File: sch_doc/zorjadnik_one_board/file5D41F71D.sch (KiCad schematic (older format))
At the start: 13 parts, among them U3 74HC595, U4 74HC595

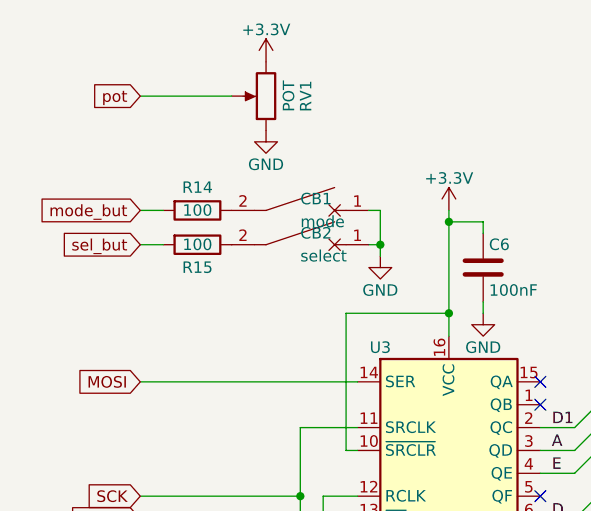
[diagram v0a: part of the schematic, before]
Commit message: полирнул меню, теперь есть функция выкючения
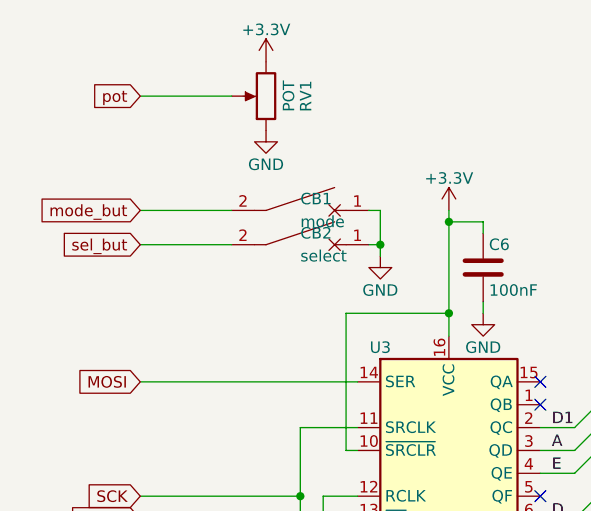
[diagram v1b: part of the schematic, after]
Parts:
- removed R14, R15: 100, Resistor_SMD:R_0805_2012Metric, symbol zorjadnik-rescue:R-Device1
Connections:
- net mode_but: now also CB1.2
- net sel_but: now also CB2.2
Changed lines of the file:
@@
 	5550 5400 5600 5400
 Connection ~ 6650 3550
-$Comp
-L zorjadnik-rescue:R-Device1 R14
-U 1 1 5D66A22A
-P 4900 1800
-F 0 "R14" V 4800 1800 50  0000 C CNN
-F 1 "100" V 4900 1800 50  0000 C CNN
-F 2 "Resistor_SMD:R_0805_2012Metric" V 4830 1800 50  0001 C CNN
-F 3 "~" H 4900 1800 50  0001 C CNN
-	1    4900 1800
-	0    1    1    0
-$EndComp
-$Comp
-L zorjadnik-rescue:R-Device1 R15
-U 1 1 5D66FFB1
-P 4900 1950
-F 0 "R15" V 5000 1950 50  0000 C CNN
-F 1 "100" V 4900 1950 50  0000 C CNN
-F 2 "Resistor_SMD:R_0805_2012Metric" V 4830 1950 50  0001 C CNN
-F 3 "~" H 4900 1950 50  0001 C CNN
-	1    4900 1950
-	0    1    1    0
-$EndComp
 Wire Wire Line
 	6400 5400 6550 5400
@@
 	4650 2550 5600 2550
 Wire Wire Line
-	4650 1950 4750 1950
+	4650 1300 5050 1300
 Wire Wire Line
-	4750 1800 4650 1800
+	4650 1800 5050 1800
 Wire Wire Line
-	4650 1300 5050 1300
+	4650 1950 5050 1950
 Wire Bus Line
 	8400 2700 8400 3550

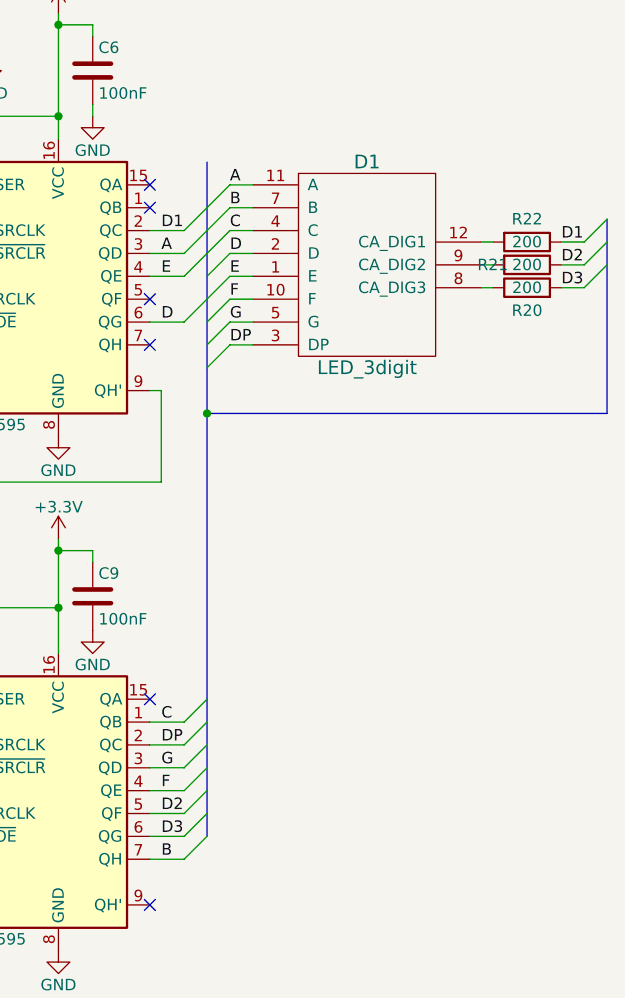
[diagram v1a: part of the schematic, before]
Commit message: список компонентов
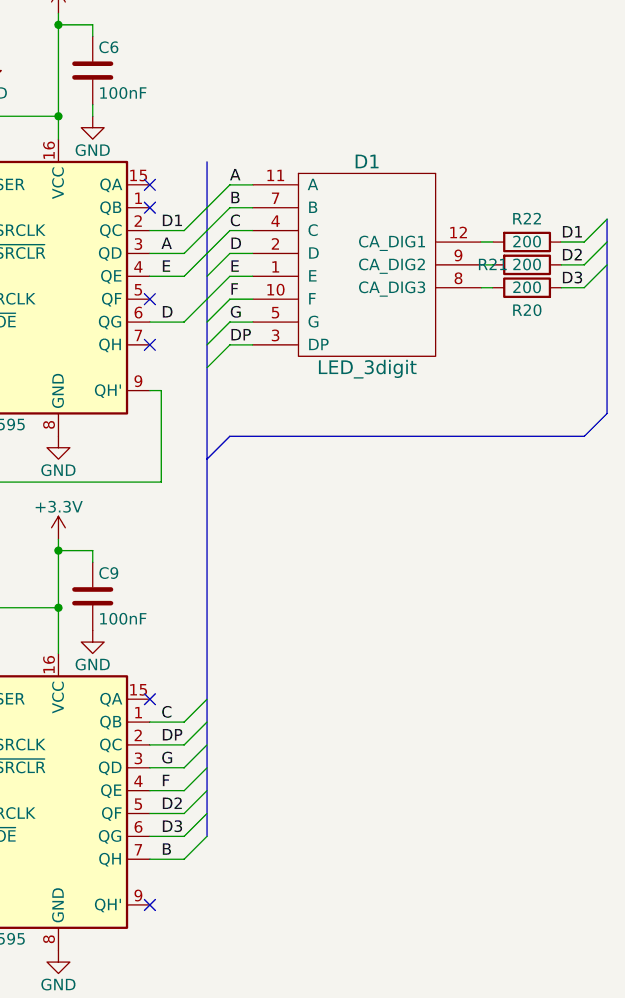
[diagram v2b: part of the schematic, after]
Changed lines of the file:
@@
 Wire Wire Line
 	5350 5000 5600 5000
-Wire Bus Line
-	6650 3550 8400 3550
 Wire Wire Line
 	6400 5200 6550 5200
@@
 Wire Wire Line
 	5550 5400 5600 5400
-Connection ~ 6650 3550
 Wire Wire Line
 	6400 5400 6550 5400
@@
 Wire Wire Line
 	4650 1950 5050 1950
+Entry Bus Bus
+	6650 3750 6750 3650
+Entry Bus Bus
+	8300 3650 8400 3550
+Wire Bus Line
+	8300 3650 6750 3650
 Wire Bus Line
 	8400 2700 8400 3550
 Wire Bus Line
-	6650 3550 6650 5400
-Wire Bus Line
-	6650 2450 6650 3550
+	6650 2450 6650 5400
 $EndSCHEMATC

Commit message: убрал сохранение настроек, не умею в такое
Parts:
- C6, C9: symbol zorjadnik-rescue:C-zorjadnik-rescue -> zorjadnik:C-zorjadnik
- CB1, CB2: symbol zorjadnik-rescue:CircuitBreaker_1P-Device1 -> zorjadnik:CircuitBreaker_1P-Device1
- R20, R21, R22: symbol zorjadnik-rescue:R-Device1 -> zorjadnik:R-Device1
- RV1: symbol zorjadnik-rescue:POT-zorjadnik-rescue -> zorjadnik:POT-zorjadnik
- U3, U4: symbol zorjadnik-rescue:74HC595-74xx1 -> zorjadnik:74HC595-74xx1
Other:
- moved on the sheet: C6, C9, CB1, CB2, D1, R20, R21, R22, RV1, U3, U4
